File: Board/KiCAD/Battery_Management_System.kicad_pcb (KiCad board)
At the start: 4 copper layers, 47.7 x 62.6 mm, 117 parts, among them J1 Conn_01x06_Socket, J10 Conn_01x02, J11 Conn_01x02, J12 Conn_01x02, J13 Conn_01x02, J2 Conn_ARM_SWD_TagConnect_TC2030, J4 Conn_01x03, J5 Conn_01x03, J7 Conn_01x05, J8 Conn_01x02, J9 Conn_01x02, Q1 AON7408, Q10 AON7407, Q2 AON7408, Q23 2N7002, Q24 2N7002, Q25 2N7002, Q26 2N7002, Q3 AON7408, Q4 AON7408, Q5 BSS83P, Q6 BSS83P, Q7 BSS83P, Q8 BSS83P, SW2 SW_Push, U1 BQ25730RSNR, U3 LTC2943CDD#PBF, U5 LMR50410, U6 INA219AxDCN, U7 INA219AxDCN, U8 INA219AxDCN, U9 STM32F103C8T6, Y1 Crystal_GND24_Small, Y4 CM8V-T1A-32.768KHZ-12.5PF-20P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

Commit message: finished PCB
PCB completed @andrewgreenberg
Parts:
- added JP1: Jumper_2_Bridged, TestPoint:TestPoint_2Pads_Pitch2.54mm_Drill0.8mm, F.Cu at (247.9, 71.5)
- moved U8 36.0 mm to (229.4, 92.3)
- moved U7 35.4 mm to (229.3, 85.3)
- moved U6 34.8 mm to (229.4, 78.6)
- moved C28 2.38 mm to (246.4, 68.5)
- moved C25 2.34 mm to (246.4, 66.2)
- moved R36 2.25 mm to (232.4, 71.4)
- moved R7 2.25 mm to (234.7, 65.4)
- moved C36 2.25 mm to (234.7, 67.2)
- moved C37 2.25 mm to (234.7, 70.7)
- moved C38 2.25 mm to (234.7, 68.8)
- moved C39 2.25 mm to (234.7, 72.2)
- moved R37 2.25 mm to (232.4, 68.0)
- moved R8 2.25 mm to (234.7, 63.9)
- moved R38 1.77 mm to (218.7, 65.4)
- moved C40 1.71 mm to (218.7, 67.2)
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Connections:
- C16 pad 1: Net-(U3-SENSE+) -> Net-(JP1-A)
- C23 pad 2: Net-(U3-SENSE+) -> Net-(JP1-A)
- C25 pad 1: Net-(U3-SENSE+) -> Net-(JP1-A)
- C28 pad 1: Net-(U3-SENSE+) -> Net-(JP1-A)
- C46 pad 1: Net-(U3-SENSE+) -> Net-(JP1-A)
- R4 pad 2: Net-(U3-SENSE+) -> Net-(JP1-A)
- R6 pad 2: Net-(U3-SENSE+) -> Net-(JP1-A)
- R76 pad 2: Net-(U3-SENSE+) -> Net-(JP1-B)
- U3 pad 1: Net-(U3-SENSE+) -> Net-(JP1-B)
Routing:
- net /Microcontroller/I2C2_SCL_To_Host: track 27.0 -> 52.8 mm, vias 2 -> 1
- net /Microcontroller/I2C2_SDA_To_Host: track 29.7 -> 55.1 mm, vias 2 -> 1
- net /Cell Interface/Cell_Balancer_1: track 26.9 -> 48.7 mm
- net SWCLK: track 26.5 -> 48.2 mm
- net 3.3V: track 62.8 -> 44.8 mm, vias 22 -> 17
- net /Microcontroller/Thermistor C4: track 39.9 -> 53.0 mm
- net Net-(U1-SW2): track 22.3 -> 9.47 mm
- net Net-(JP1-B): track 0.00 -> 11.3 mm
- net /Cell Interface/Cell_Balancer_4: track 43.8 -> 34.2 mm
- net /Charge Control/VBus: track 67.9 -> 77.2 mm
- net /Microcontroller/USART1_TX: track 37.2 -> 46.3 mm
- net SWDIO: track 40.0 -> 49.0 mm
- net VDDA: track 33.0 -> 25.0 mm
- net /Microcontroller/Thermistor C2: track 35.0 -> 43.0 mm, vias 0 -> 1
- net /Cell Interface/SDA: track 64.9 -> 71.9 mm, vias 9 -> 3
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- added copper zone on F.Cu, net Net-(JP1-A)
- added copper zone on F.Cu, net Net-(Q25-D)
- added copper zone on F.Cu, net Net-(Q26-D)
- added copper zone on F.Cu, net Net-(U1-ILIM_HIZ)
- added copper zone on F.Cu, net Net-(U1-SW2)
- removed copper zone on F.Cu, net Net-(U3-SENSE+)
- removed copper zone on F.Cu, net Net-(U9-PD0_OSC_IN)

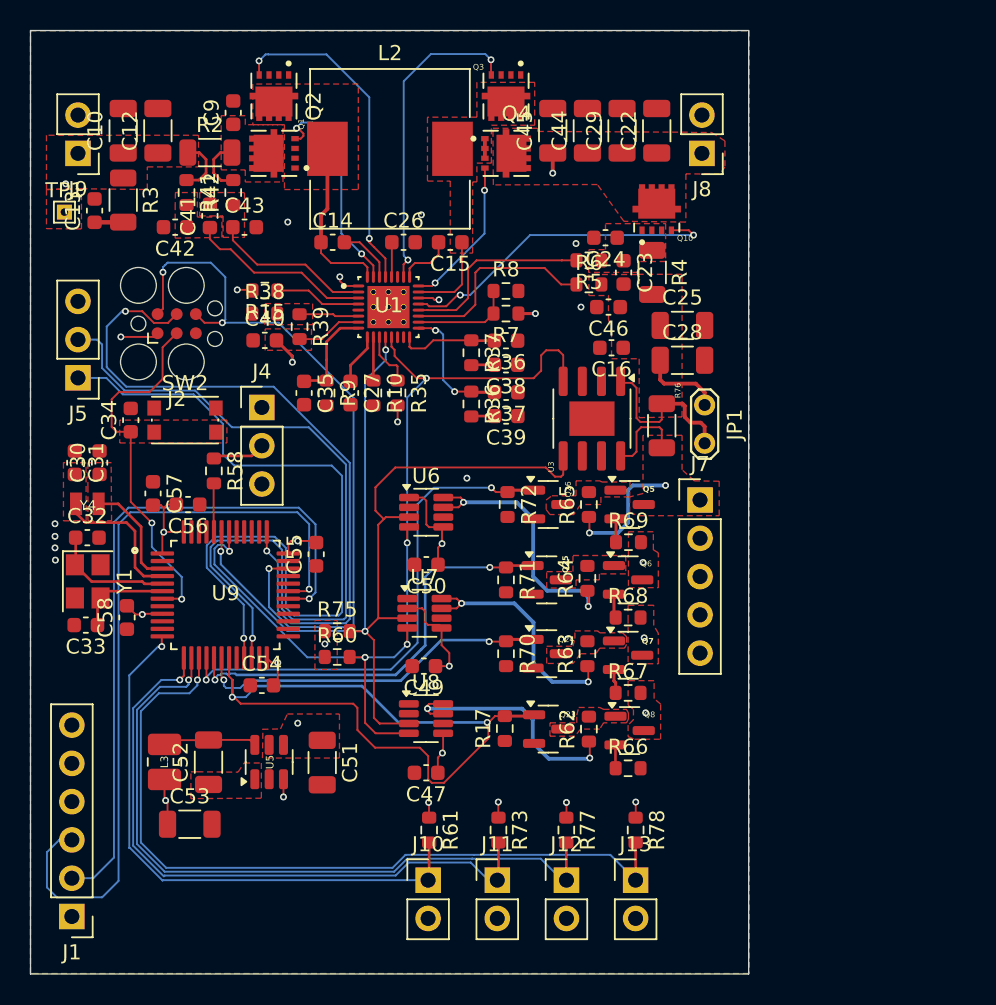
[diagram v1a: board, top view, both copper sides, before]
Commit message: revised PCB
This design accounts for majority of the updates requested by Faculty Advisor

@KeytarGoblin  @andrewgreenberg
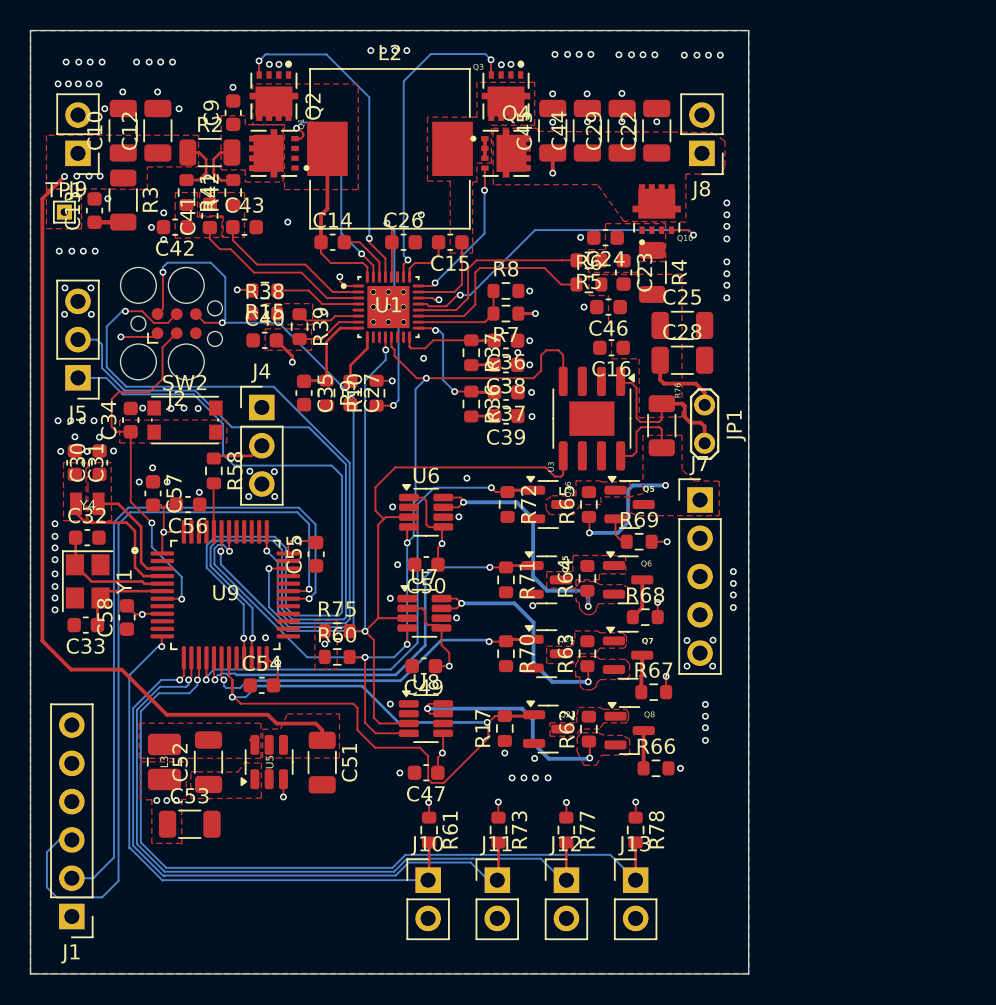
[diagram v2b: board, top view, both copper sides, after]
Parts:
- removed R35: 10k, Resistor_SMD:R_0603_1608Metric
- R10: value 30k -> 10
- R9: value 200k -> 187k
- moved R66 1.85 mm to (244.7, 95.6)
- moved R67 1.70 mm to (244.5, 90.6)
- moved R68 1.14 mm to (243.9, 85.6)
- moved R69 0.71 mm to (243.5, 80.6)
- moved R10 0.21 mm to (226.1, 70.7), turned to 90 degrees
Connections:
- Q6 pad 2: Net-(Q6-S) -> /Cell Interface/Cell 3
- Q6 pad 3: /Cell Interface/Cell 3 -> Net-(Q6-D)
- Q7 pad 2: Net-(Q7-S) -> /Cell Interface/Cell 2
- Q7 pad 3: /Cell Interface/Cell 2 -> Net-(Q7-D)
- Q8 pad 2: Net-(Q8-S) -> /Cell Interface/Cell 1
- Q8 pad 3: /Cell Interface/Cell 1 -> Net-(Q8-D)
- R10 pad 1: Net-(U1-PSYS) -> Net-(U1-REGN)
- R10 pad 2: GND -> VDDA
- R66 pad 1: Net-(Q8-S) -> Net-(Q8-D)
- R67 pad 1: Net-(Q7-S) -> Net-(Q7-D)
- R68 pad 1: Net-(Q6-S) -> Net-(Q6-D)
- U1 pad 10: Net-(U1-PSYS) -> unconnected-(TP3-Pad1)
- U1 pad 11: Net-(U1-~{PROCHOT}) -> unconnected-(TP2-Pad1)
- U1 pad 5: /Charge Control/OTG/VAP -> GND
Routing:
- net Net-(U1-REGN): track 2.35 -> 17.4 mm, vias 0 -> 2
- net VDDA: track 25.0 -> 30.4 mm, vias 2 -> 3
- net Net-(U5-SW): track 5.89 -> 0.87 mm
- net 3.3V: track 44.8 -> 40.6 mm, vias 17 -> 18
- net Net-(U1-~{PROCHOT}): track 3.97 -> 0.00 mm
- net /Charge Control/VBus: track 77.2 -> 80.2 mm, vias 3 -> 5
- net Net-(U1-PSYS): track 2.88 -> 0.00 mm
- net Net-(Q6-D): track 0.00 -> 2.73 mm
- net Net-(Q8-D): track 0.00 -> 2.51 mm
- net Net-(Q7-D): track 0.00 -> 2.48 mm
- net Net-(Q7-S): track 1.76 -> 0.00 mm
- net Net-(Q6-S): track 1.60 -> 0.00 mm
- net Net-(Q8-S): track 1.57 -> 0.00 mm
- net /Cell Interface/Cell 3: track 27.5 -> 28.7 mm
- net /Cell Interface/Cell 1: track 30.5 -> 31.6 mm
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- added copper zone on F.Cu, net Net-(U5-SW)

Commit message: Silkscreen text minimized, added logo
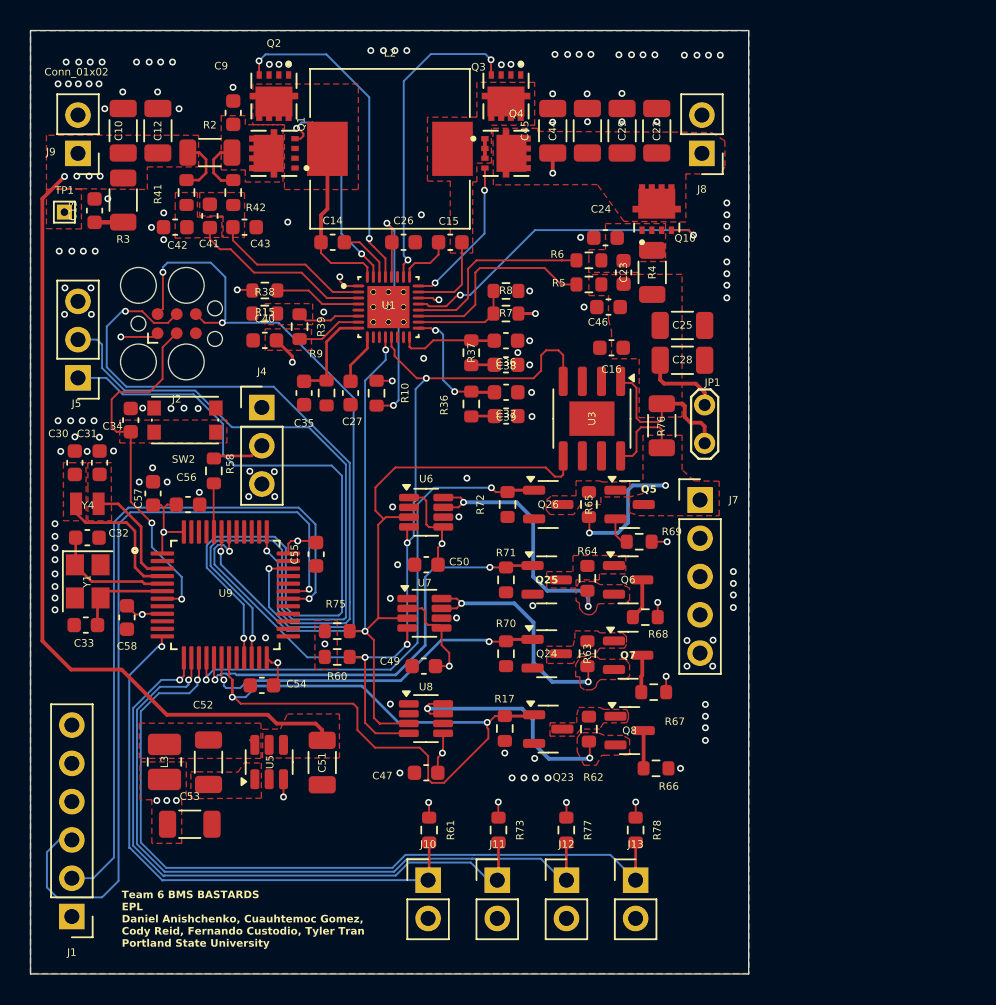
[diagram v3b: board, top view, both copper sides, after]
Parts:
- J2: value Conn_ARM_SWD_TagConnect_TC2030 -> Conn_ARM_SWD
- TP1: value TestPoint_Small -> TST_PNT_S
- Y4: value CM8V-T1A-32.768KHZ-12.5PF-20PPM-TA-QA -> CM8V-T1A
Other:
- board text added: "Team 6 BMS BASTARDS EPL Daniel Anishchenko, Cuauhtemoc Gomez, Cody Reid, Fernando Custodio, Tyler Tran Portland State University"

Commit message: Team #6 - Battery Management Module Rev 1 - PCB
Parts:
- removed C24, C46: 0.1uF, Capacitor_SMD:C_0603_1608Metric
- removed R8: 350k, Resistor_SMD:R_0603_1608Metric
- added TP14: TestPoint_Small, TestPoint:TestPoint_THTPad_1.0x1.0mm_Drill0.5mm, F.Cu at (233.6, 75.6)
- added TP15: TestPoint_Small, TestPoint:TestPoint_THTPad_1.0x1.0mm_Drill0.5mm, F.Cu at (233.0, 80.8)
- added TP16: TestPoint_Small, TestPoint:TestPoint_THTPad_1.0x1.0mm_Drill0.5mm, F.Cu at (233.0, 85.7)
- added TP17: TestPoint_Small, TestPoint:TestPoint_THTPad_1.0x1.0mm_Drill0.5mm, F.Cu at (232.9, 90.5)
- added TP2: TestPoint_Small, TestPoint:TestPoint_THTPad_1.0x1.0mm_Drill0.5mm, F.Cu at (225.5, 74.0)
- added TP24: TestPoint_Small, TestPoint:TestPoint_THTPad_1.0x1.0mm_Drill0.5mm, F.Cu at (222.5, 77.4)
- added TP25: TestPoint_Small, TestPoint:TestPoint_THTPad_1.0x1.0mm_Drill0.5mm, F.Cu at (221.4, 74.4)
- added TP26: TestPoint_Small, TestPoint:TestPoint_THTPad_1.0x1.0mm_Drill0.5mm, F.Cu at (204.7, 89.8)
- added TP27: TestPoint_Small, TestPoint:TestPoint_THTPad_1.0x1.0mm_Drill0.5mm, F.Cu at (216.2, 49.2)
- added TP28: TestPoint_Small, TestPoint:TestPoint_THTPad_1.0x1.0mm_Drill0.5mm, F.Cu at (237.7, 49.4)
- added TP3: TestPoint_Small, TestPoint:TestPoint_THTPad_1.0x1.0mm_Drill0.5mm, F.Cu at (225.5, 76.0)
- added TP39: TestPoint_Small, TestPoint:TestPoint_THTPad_1.0x1.0mm_Drill0.5mm, F.Cu at (220.0, 98.7)
- added TP4: TestPoint_Small, TestPoint:TestPoint_THTPad_1.0x1.0mm_Drill0.5mm, F.Cu at (218.5, 68.9)
- added TP5: TestPoint_Small, TestPoint:TestPoint_THTPad_1.0x1.0mm_Drill0.5mm, F.Cu at (230.1, 68.7)
- added TP6: TestPoint_Small, TestPoint:TestPoint_THTPad_1.0x1.0mm_Drill0.5mm, F.Cu at (219.2, 62.2)
- added TP7: TestPoint_Small, TestPoint:TestPoint_THTPad_1.0x1.0mm_Drill0.5mm, F.Cu at (225.5, 83.0)
- added TP8: TestPoint_Small, TestPoint:TestPoint_THTPad_1.0x1.0mm_Drill0.5mm, F.Cu at (224.1, 91.1)
- J2: value Conn_ARM_SWD -> Conn_ARM_SWD_TagConnect_TC2030
- R7: value 350k -> 33k
- TP1: value TST_PNT_S -> TestPoint_Small
- Y4: value CM8V-T1A -> CM8V-T1A-32.768KHZ-12.5PF-20PPM-TA-QA
- moved J7 0.84 mm to (248.4, 77.8)
- moved C40 0.10 mm to (218.7, 67.1)
- moved C27 0.08 mm to (224.3, 70.7)
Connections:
- R7 pad 2: Net-(U1-CELL_BATPRESZ) -> GND
- U1 pad 18: Net-(U1-CELL_BATPRESZ) -> GND
- U9 pad 11: unconnected-(U9-PA1-Pad11) -> /Charge Control/CHRG_OK
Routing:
- net /Charge Control/CHRG_OK: track 5.75 -> 82.3 mm, vias 0 -> 1
- net GND: track 0.07 -> 16.0 mm
- net unconnected-(TP3-Pad1): track 0.00 -> 10.4 mm, vias 0 -> 1
- net unconnected-(TP2-Pad1): track 0.00 -> 7.49 mm
- net Net-(U1-CELL_BATPRESZ): track 6.71 -> 0.00 mm
- net Net-(U1-SW2): track 9.47 -> 13.6 mm
- net /Cell Interface/SDA: track 71.9 -> 75.9 mm
- net Net-(U1-SW1): track 12.2 -> 16.1 mm
- net /Cell Interface/SCL: track 64.7 -> 67.9 mm
- net /Microcontroller/I2C2_SDA_To_Host: track 55.1 -> 57.5 mm
- net /Cell Interface/Cell_Balancer_3: track 28.7 -> 30.7 mm
- net /Cell Interface/Cell_Balancer_2: track 24.2 -> 25.9 mm
- net /Microcontroller/I2C2_SCL_To_Host: track 52.8 -> 54.5 mm
- net /Cell Interface/Cell_Balancer_4: track 34.2 -> 35.7 mm
- net /Charge Control/VBus: track 80.2 -> 81.7 mm
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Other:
- board text added: "Team #6 EPL Battery Management System Rev 1 Daniel Anishchenko, Cuauhtemoc Gomez, Cody Reid, Fernando Custodio, Tyler Tran Portland State University"
- board text removed: "Team 6 BMS BASTARDS EPL Daniel Anishchenko, Cuauhtemoc Gomez, Cody Reid, Fernando Custodio, Tyler Tran Portland State University"

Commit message: Edits to PCB
@andrewgreenberg @KeytarGoblin
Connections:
- TP2 pad 1: unconnected-(TP2-Pad1) -> Net-(U1-~{PROCHOT})
- TP3 pad 1: unconnected-(TP3-Pad1) -> Net-(U1-PSYS)
- U1 pad 10: unconnected-(TP3-Pad1) -> Net-(U1-PSYS)
- U1 pad 11: unconnected-(TP2-Pad1) -> Net-(U1-~{PROCHOT})
- U1 pad 33: (no net) -> GND
- U1 pad 34: (no net) -> GND
- U1 pad 35: (no net) -> GND
- U1 pad 36: (no net) -> GND
- U1 pad 37: (no net) -> GND
- U1 pad 38: (no net) -> GND
- U1 pad 39: (no net) -> GND
- U1 pad 40: (no net) -> GND
- U1 pad 41: (no net) -> GND
- U1 pad 42: (no net) -> GND
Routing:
- net unconnected-(TP3-Pad1): track 10.4 -> 0.00 mm, vias 1 -> 0
- net Net-(U1-PSYS): track 0.00 -> 10.4 mm, vias 0 -> 1
- net GND: track 16.0 -> 24.3 mm, vias 137 -> 138
- net unconnected-(TP2-Pad1): track 7.49 -> 0.00 mm
- net Net-(U1-~{PROCHOT}): track 0.00 -> 7.49 mm
- net Net-(U1-REGN): track 17.6 -> 19.3 mm
- net Net-(U1-ILIM_HIZ): track 4.23 -> 5.72 mm
- net /Cell Interface/Cell_Balancer_1: track 50.1 -> 50.7 mm
- removed copper zone on F.Cu, net Net-(U1-ILIM_HIZ)

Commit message: Final Polish
@KeytarGoblin  @andrewgreenberg
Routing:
- net /Cell Interface/Cell_Balancer_1: track 50.7 -> 51.3 mm
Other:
- outline, holes or cut-outs redrawn

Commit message: PCB Revision
PCN near full completion, currently running on no errors while running DRC.

@KeytarGoblin @andrewgreenberg @Danish2PSU
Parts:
- moved C47 4.56 mm to (226.5, 92.4), turned to 90 degrees
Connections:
- U6 pad 1: 3.3V -> /Cell Interface/Cell 3
- U6 pad 2: GND -> /Cell Interface/Cell 3
- U6 pad 3: /Cell Interface/SDA -> GND
- U6 pad 4: /Cell Interface/SCL -> 3.3V
- U6 pad 5: 3.3V -> /Cell Interface/SCL
- U6 pad 6: GND -> /Cell Interface/SDA
- U6 pad 7: /Cell Interface/Cell 3 -> GND
- U6 pad 8: /Cell Interface/Cell 3 -> 3.3V
- U7 pad 1: GND -> /Cell Interface/Cell 2
- U7 pad 2: 3.3V -> /Cell Interface/Cell 2
- U7 pad 3: /Cell Interface/SDA -> GND
- U7 pad 4: /Cell Interface/SCL -> 3.3V
- U7 pad 5: 3.3V -> /Cell Interface/SCL
- U7 pad 6: GND -> /Cell Interface/SDA
- U7 pad 7: /Cell Interface/Cell 2 -> 3.3V
- U7 pad 8: /Cell Interface/Cell 2 -> GND
- U8 pad 1: GND -> /Cell Interface/Cell 1
- U8 pad 2: GND -> /Cell Interface/Cell 1
- U8 pad 3: /Cell Interface/SDA -> GND
- U8 pad 4: /Cell Interface/SCL -> 3.3V
- U8 pad 5: 3.3V -> /Cell Interface/SCL
- U8 pad 6: GND -> /Cell Interface/SDA
- U8 pad 7: /Cell Interface/Cell 1 -> GND
- U8 pad 8: /Cell Interface/Cell 1 -> GND
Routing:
- net /Cell Interface/Cell_Balancer_1: track 51.3 -> 27.7 mm
- net /Cell Interface/SDA: track 75.8 -> 88.7 mm
- net /Cell Interface/SCL: track 67.9 -> 76.6 mm
- net 3.3V: track 41.8 -> 47.3 mm
- net GND: track 24.3 -> 27.2 mm, vias 138 -> 137
- net /Cell Interface/Cell 3: track 28.7 -> 31.1 mm
- net /Cell Interface/Cell 2: track 28.8 -> 31.0 mm
- net /Cell Interface/Cell 1: track 31.6 -> 32.1 mm
